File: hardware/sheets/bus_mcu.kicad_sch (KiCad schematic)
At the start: 22 parts, among them U1 RP2350B, U10 74HC163, U11 74HC163, U12 74HC165, U2 74LVC245A, U3 74LVC245A, U4 74LVC245A, U5 74LVC245A, U6 74LVC245A, U7 74HC163, U8 74HC163, U9 74HC163

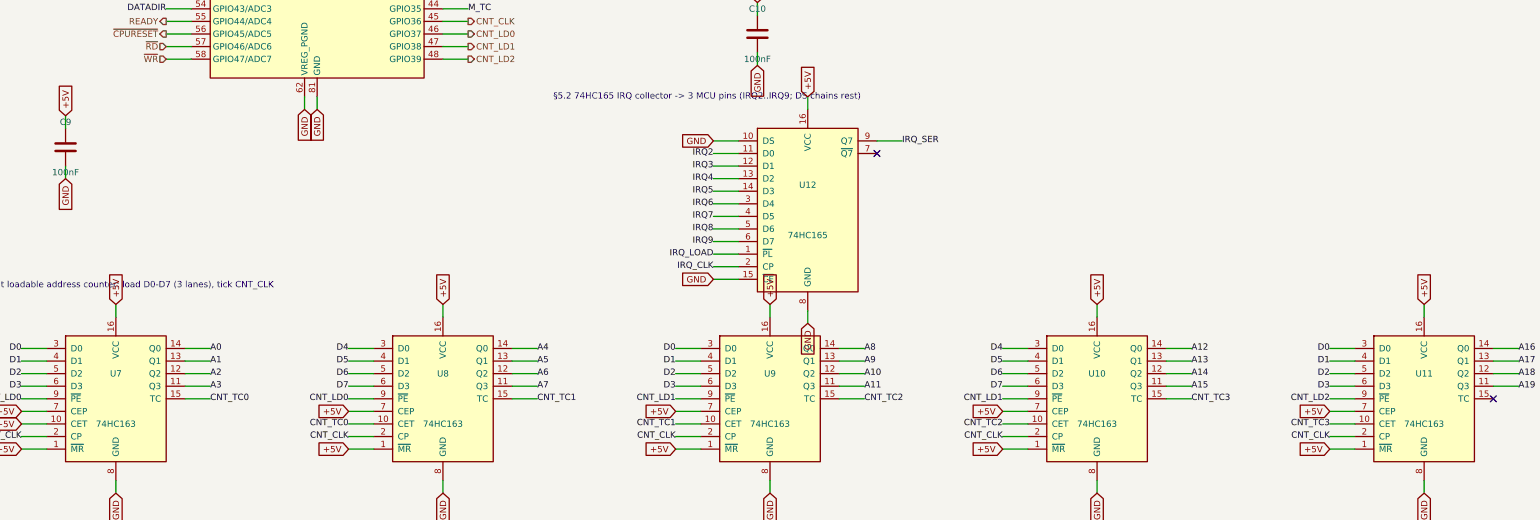
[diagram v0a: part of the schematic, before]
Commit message: Standardize 5V glue on 74HCT; fix bus-latch family; div-3 -> 74HCT163
All 5V 74-series logic moved from mixed HC/HCT to 74HCT (TTL thresholds reliably
read 3.3V level-shifter outputs). Fixes the address latches / data transceiver
that were wrongly 74HC instead of the design's 74HCT. The div-by-3 moves from
74HC4017 (no HCT variant) to a 74HCT163 preset-to-3 with a spare 74HCT04 gate
for the TC->~PE reload. Per-card level shifters use a dedicated 74LVC245A symbol.
Pinouts unchanged; netlist intact; zero structural ERC errors.

Co-Authored-By: Claude Opus 4.8 (1M context) <noreply@anthropic.com>
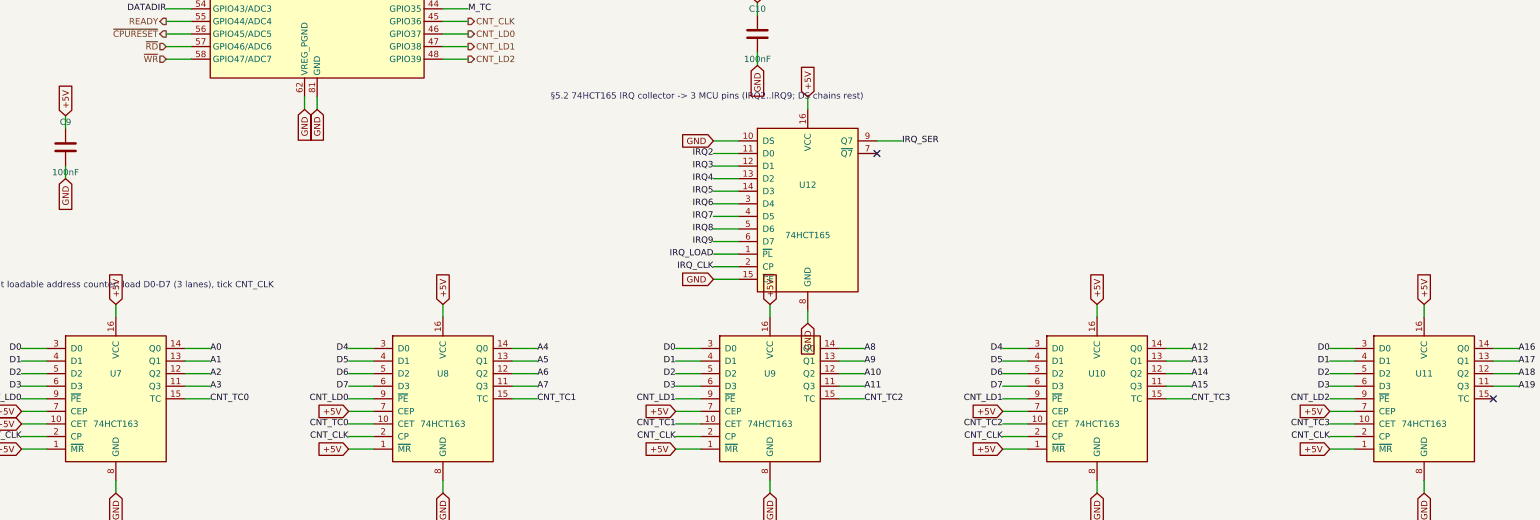
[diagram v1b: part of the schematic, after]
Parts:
- removed U10, U11, U7, U8, U9: 74HC163, symbol mini-xt:74HC163
- removed U12: 74HC165, symbol mini-xt:74HC165
- removed U2, U3, U4, U5, U6: 74LVC245A, symbol mini-xt:74HC245
- added U10, U11, U7, U8, U9: 74HCT163, symbol mini-xt:74HCT163
- added U12: 74HCT165, symbol mini-xt:74HCT165
- added U2, U3, U4, U5, U6: 74LVC245A, symbol mini-xt:74LVC245A
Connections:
- net +3V3: now also U2.20 (VCC), U3.20 (VCC), U4.20 (VCC), U5.20 (VCC), U6.20 (VCC)
- net +5V: now also U10.1 (~{MR}), U10.16 (VCC), U10.7 (CEP), U11.1 (~{MR}), U11.16 (VCC), U11.7 (CEP), U12.16 (VCC), U7.1 (~{MR}), U7.10 (CET), U7.16 (VCC), U7.7 (CEP), U8.1 (~{MR}), U8.16 (VCC), U8.7 (CEP), U9.1 (~{MR}), U9.16 (VCC), U9.7 (CEP)
- net A0: now also U3.18 (B0), U7.14 (Q0)
- net A1: now also U3.17 (B1), U7.13 (Q1)
- net A10: now also U4.16 (B2), U9.12 (Q2)
- net A11: now also U4.15 (B3), U9.11 (Q3)
- net A12: now also U10.14 (Q0), U4.14 (B4)
- net A13: now also U10.13 (Q1), U4.13 (B5)
- net A14: now also U10.12 (Q2), U4.12 (B6)
- net A15: now also U10.11 (Q3), U4.11 (B7)
- net A16: now also U11.14 (Q0), U5.18 (B0)
- net A17: now also U11.13 (Q1), U5.17 (B1)
- net A18: now also U11.12 (Q2), U5.16 (B2)
- net A19: now also U11.11 (Q3), U5.15 (B3)
- net A2: now also U3.16 (B2), U7.12 (Q2)
- net A3: now also U3.15 (B3), U7.11 (Q3)
- net A4: now also U3.14 (B4), U8.14 (Q0)
- net A5: now also U3.13 (B5), U8.13 (Q1)
- net A6: now also U3.12 (B6), U8.12 (Q2)
- net A7: now also U3.11 (B7), U8.11 (Q3)
- net A8: now also U4.18 (B0), U9.14 (Q0)
- net A9: now also U4.17 (B1), U9.13 (Q1)
- net AEN: now also U6.14 (B4)
- net BALE: now also U6.11 (B7)
- net BUSDIR: now also U3.1 (A->B), U4.1 (A->B), U5.1 (A->B), U6.1 (A->B)
- net CNT_CLK: now also U10.2 (CP), U11.2 (CP), U7.2 (CP), U8.2 (CP), U9.2 (CP)
- net CNT_LD0: now also U7.9 (~{PE}), U8.9 (~{PE})
- net CNT_LD1: now also U10.9 (~{PE}), U9.9 (~{PE})
- net CNT_LD2: now also U11.9 (~{PE})
- net CNT_TC0: now also U7.15 (TC), U8.10 (CET)
- net CNT_TC1: now also U8.15 (TC), U9.10 (CET)
- net CNT_TC2: now also U10.10 (CET), U9.15 (TC)
- net CNT_TC3: now also U10.15 (TC), U11.10 (CET)
- net D0: now also U11.3 (D0), U2.18 (B0), U7.3 (D0), U9.3 (D0)
- net D1: now also U11.4 (D1), U2.17 (B1), U7.4 (D1), U9.4 (D1)
- net D2: now also U11.5 (D2), U2.16 (B2), U7.5 (D2), U9.5 (D2)
- net D3: now also U11.6 (D3), U2.15 (B3), U7.6 (D3), U9.6 (D3)
- net D4: now also U10.3 (D0), U2.14 (B4), U8.3 (D0)
- net D5: now also U10.4 (D1), U2.13 (B5), U8.4 (D1)
- net D6: now also U10.5 (D2), U2.12 (B6), U8.5 (D2)
- net D7: now also U10.6 (D3), U2.11 (B7), U8.6 (D3)
- net DATADIR: now also U2.1 (A->B)
- net GND: now also U10.8 (GND), U11.8 (GND), U12.10 (DS), U12.15 (~{CE}), U12.8 (GND), U2.10 (GND), U2.19 (CE), U3.10 (GND), U3.19 (CE), U4.10 (GND), U4.19 (CE), U5.10 (GND), U5.19 (CE), U6.10 (GND), U6.19 (CE), U7.8 (GND), U8.8 (GND), U9.8 (GND)
- net IRQ2: now also U12.11 (D0)
- net IRQ3: now also U12.12 (D1)
- net IRQ4: now also U12.13 (D2)
- net IRQ5: now also U12.14 (D3)
- net IRQ6: now also U12.3 (D4)
- net IRQ7: now also U12.4 (D5)
- net IRQ8: now also U12.5 (D6)
- net IRQ9: now also U12.6 (D7)
- net IRQ_CLK: now also U12.2 (CP)
- net IRQ_LOAD: now also U12.1 (~{PL})
- net IRQ_SER: now also U12.9 (Q7)
- net MA0: now also U3.2 (A0)
- net MA1: now also U3.3 (A1)
- net MA10: now also U4.4 (A2)
- net MA11: now also U4.5 (A3)
- net MA12: now also U4.6 (A4)
- net MA13: now also U4.7 (A5)
- net MA14: now also U4.8 (A6)
- net MA15: now also U4.9 (A7)
- net MA16: now also U5.2 (A0)
- net MA17: now also U5.3 (A1)
- net MA18: now also U5.4 (A2)
- net MA19: now also U5.5 (A3)
- net MA2: now also U3.4 (A2)
- net MA3: now also U3.5 (A3)
- net MA4: now also U3.6 (A4)
- net MA5: now also U3.7 (A5)
- net MA6: now also U3.8 (A6)
- net MA7: now also U3.9 (A7)
- net MA8: now also U4.2 (A0)
- net MA9: now also U4.3 (A1)
- net MD0: now also U2.2 (A0)
- net MD1: now also U2.3 (A1)
- net MD2: now also U2.4 (A2)
- net MD3: now also U2.5 (A3)
- net MD4: now also U2.6 (A4)
- net MD5: now also U2.7 (A5)
- net MD6: now also U2.8 (A6)
- net MD7: now also U2.9 (A7)
- net M_AEN: now also U6.6 (A4)
- net M_BALE: now also U6.9 (A7)
- net M_IOR: now also U6.2 (A0)
- net M_IOW: now also U6.3 (A1)
- net M_MEMR: now also U6.4 (A2)
- net M_MEMW: now also U6.5 (A3)
- net M_RESETDRV: now also U6.7 (A5)
- net M_TC: now also U6.8 (A6)
- net RESET_DRV: now also U6.13 (B5)
- net TC: now also U6.12 (B6)
- net ~{IOR}: now also U6.18 (B0)
- net ~{IOW}: now also U6.17 (B1)
- net ~{MEMR}: now also U6.16 (B2)
- net ~{MEMW}: now also U6.15 (B3)
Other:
- note added: "§5.2 74HCT165 IRQ collector -> 3 MCU pins (IRQ2..IRQ9; DS chains rest)"
- note removed: "§5.2 74HC165 IRQ collector -> 3 MCU pins (IRQ2..IRQ9; DS chains rest)"
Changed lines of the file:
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@@
 		(at 214.63 222.25)
 	)
-	(text "§5.2 74HC165 IRQ collector -> 3 MCU pins (IRQ2..IRQ9; DS chains rest)"
+	(text "§5.2 74HCT165 IRQ collector -> 3 MCU pins (IRQ2..IRQ9; DS chains rest)"
 		(at 180.34 210.82 0)
 		(effects
@@
 		(instances
 			(project "mini-xt"
-				(path "/d5fb706d-3720-437f-850e-91a8fdce298f/59d1bc93-8348-4a37-b005-a2b2152d1bab"
+				(path "/12a90590-121b-4b08-bc73-62c223de1072/e50d0a17-50fb-4006-9356-a8363e32698a"
 					(reference "U201")
 					(unit 1)
@@
 	)
 	(symbol
-		(lib_id "mini-xt:74HC245")
+		(lib_id "mini-xt:74LVC245A")
 		(at 200.66 76.2 0)
 		(unit 1)
@@
 		(instances
 			(project "mini-xt"
-				(path "/d5fb706d-3720-437f-850e-91a8fdce298f/59d1bc93-8348-4a37-b005-a2b2152d1bab"
+				(path "/12a90590-121b-4b08-bc73-62c223de1072/e50d0a17-50fb-4006-9356-a8363e32698a"
 					(reference "U202")
 					(unit 1)
@@
 	)
 	(symbol
-		(lib_id "mini-xt:74HC245")
+		(lib_id "mini-xt:74LVC245A")
 		(at 200.66 152.4 0)
 		(unit 1)
@@
 		(instances
 			(project "mini-xt"
-				(path "/d5fb706d-3720-437f-850e-91a8fdce298f/59d1bc93-8348-4a37-b005-a2b2152d1bab"
+				(path "/12a90590-121b-4b08-bc73-62c223de1072/e50d0a17-50fb-4006-9356-a8363e32698a"
 					(reference "U206")
 					(unit 1)
@@
 	)
 	(symbol
-		(lib_id "mini-xt:74HC245")
+		(lib_id "mini-xt:74LVC245A")
 		(at 281.94 76.2 0)
 		(unit 1)
@@
 		(instances
 			(project "mini-xt"
-				(path "/d5fb706d-3720-437f-850e-91a8fdce298f/59d1bc93-8348-4a37-b005-a2b2152d1bab"
+				(path "/12a90590-121b-4b08-bc73-62c223de1072/e50d0a17-50fb-4006-9356-a8363e32698a"
 					(reference "U203")
 					(unit 1)
@@
 	)
 	(symbol
-		(lib_id "mini-xt:74HC245")
+		(lib_id "mini-xt:74LVC245A")
 		(at 358.14 76.2 0)
 		(unit 1)
@@
 		(instances
 			(project "mini-xt"
-				(path "/d5fb706d-3720-437f-850e-91a8fdce298f/59d1bc93-8348-4a37-b005-a2b2152d1bab"
+				(path "/12a90590-121b-4b08-bc73-62c223de1072/e50d0a17-50fb-4006-9356-a8363e32698a"
 					(reference "U204")
 					(unit 1)
@@
 	)
 	(symbol
-		(lib_id "mini-xt:74HC245")
+		(lib_id "mini-xt:74LVC245A")
 		(at 281.94 152.4 0)
 		(unit 1)
@@
 		(instances
 			(project "mini-xt"
-				(path "/d5fb706d-3720-437f-850e-91a8fdce298f/59d1bc93-8348-4a37-b005-a2b2152d1bab"
+				(path "/12a90590-121b-4b08-bc73-62c223de1072/e50d0a17-50fb-4006-9356-a8363e32698a"
 					(reference "U205")
 					(unit 1)
@@
 	)
 	(symbol
-		(lib_id "mini-xt:74HC163")
+		(lib_id "mini-xt:74HCT163")
 		(at 60.96 271.78 0)
 		(unit 1)
@@
 			)
 		)
-		(property "Value" "74HC163"
+		(property "Value" "74HCT163"
 			(at 60.96 276.86 0)
 			(effects
@@
 		(instances
 			(project "mini-xt"
-				(path "/d5fb706d-3720-437f-850e-91a8fdce298f/59d1bc93-8348-4a37-b005-a2b2152d1bab"
+				(path "/12a90590-121b-4b08-bc73-62c223de1072/e50d0a17-50fb-4006-9356-a8363e32698a"
 					(reference "U207")
 					(unit 1)
@@
 	)
 	(symbol
-		(lib_id "mini-xt:74HC163")
+		(lib_id "mini-xt:74HCT163")
 		(at 127 271.78 0)
 		(unit 1)
@@
 			)
 		)
-		(property "Value" "74HC163"
+		(property "Value" "74HCT163"
 			(at 127 276.86 0)
 			(effects
@@
 		(instances
 			(project "mini-xt"
-				(path "/d5fb706d-3720-437f-850e-91a8fdce298f/59d1bc93-8348-4a37-b005-a2b2152d1bab"
+				(path "/12a90590-121b-4b08-bc73-62c223de1072/e50d0a17-50fb-4006-9356-a8363e32698a"
 					(reference "U208")
 					(unit 1)
@@
 	)
 	(symbol
-		(lib_id "mini-xt:74HC163")
+		(lib_id "mini-xt:74HCT163")
 		(at 193.04 271.78 0)
 		(unit 1)
@@
 			)
 		)
-		(property "Value" "74HC163"
+		(property "Value" "74HCT163"
 			(at 193.04 276.86 0)
 			(effects
@@
 		(instances
 			(project "mini-xt"
-				(path "/d5fb706d-3720-437f-850e-91a8fdce298f/59d1bc93-8348-4a37-b005-a2b2152d1bab"
+				(path "/12a90590-121b-4b08-bc73-62c223de1072/e50d0a17-50fb-4006-9356-a8363e32698a"
 					(reference "U209")
 					(unit 1)
@@
 	)
 	(symbol
-		(lib_id "mini-xt:74HC163")
+		(lib_id "mini-xt:74HCT163")
 		(at 259.08 271.78 0)
 		(unit 1)
@@
 			)
 		)
-		(property "Value" "74HC163"
+		(property "Value" "74HCT163"
 			(at 259.08 276.86 0)
 			(effects
@@
 		(instances
 			(project "mini-xt"
-				(path "/d5fb706d-3720-437f-850e-91a8fdce298f/59d1bc93-8348-4a37-b005-a2b2152d1bab"
+				(path "/12a90590-121b-4b08-bc73-62c223de1072/e50d0a17-50fb-4006-9356-a8363e32698a"
 					(reference "U210")
 					(unit 1)
@@
 	)
 	(symbol
-		(lib_id "mini-xt:74HC163")
+		(lib_id "mini-xt:74HCT163")
 		(at 325.12 271.78 0)
 		(unit 1)
@@
 			)
 		)
-		(property "Value" "74HC163"
+		(property "Value" "74HCT163"
 			(at 325.12 276.86 0)
 			(effects
@@
 		(instances
 			(project "mini-xt"
-				(path "/d5fb706d-3720-437f-850e-91a8fdce298f/59d1bc93-8348-4a37-b005-a2b2152d1bab"
+				(path "/12a90590-121b-4b08-bc73-62c223de1072/e50d0a17-50fb-4006-9356-a8363e32698a"
 					(reference "U211")
 					(unit 1)
@@
 	)
 	(symbol
-		(lib_id "mini-xt:74HC165")
+		(lib_id "mini-xt:74HCT165")
 		(at 200.66 233.68 0)
 		(unit 1)
@@
 			)
 		)
-		(property "Value" "74HC165"
+		(property "Value" "74HCT165"
 			(at 200.66 238.76 0)
 			(effects
@@
 		(instances
 			(project "mini-xt"
-				(path "/d5fb706d-3720-437f-850e-91a8fdce298f/59d1bc93-8348-4a37-b005-a2b2152d1bab"
+				(path "/12a90590-121b-4b08-bc73-62c223de1072/e50d0a17-50fb-4006-9356-a8363e32698a"
 					(reference "U212")
 					(unit 1)
@@
 		(instances
 			(project "mini-xt"
-				(path "/d5fb706d-3720-437f-850e-91a8fdce298f/59d1bc93-8348-4a37-b005-a2b2152d1bab"
+				(path "/12a90590-121b-4b08-bc73-62c223de1072/e50d0a17-50fb-4006-9356-a8363e32698a"
 					(reference "C201")
 					(unit 1)
@@
 		(instances
 			(project "mini-xt"
-				(path "/d5fb706d-3720-437f-850e-91a8fdce298f/59d1bc93-8348-4a37-b005-a2b2152d1bab"
+				(path "/12a90590-121b-4b08-bc73-62c223de1072/e50d0a17-50fb-4006-9356-a8363e32698a"
 					(reference "C202")
 					(unit 1)
@@
 		(instances
 			(project "mini-xt"
-				(path "/d5fb706d-3720-437f-850e-91a8fdce298f/59d1bc93-8348-4a37-b005-a2b2152d1bab"
+				(path "/12a90590-121b-4b08-bc73-62c223de1072/e50d0a17-50fb-4006-9356-a8363e32698a"
 					(reference "C203")
 					(unit 1)
@@
 		(instances
 			(project "mini-xt"
-				(path "/d5fb706d-3720-437f-850e-91a8fdce298f/59d1bc93-8348-4a37-b005-a2b2152d1bab"
+				(path "/12a90590-121b-4b08-bc73-62c223de1072/e50d0a17-50fb-4006-9356-a8363e32698a"
 					(reference "C204")
 					(unit 1)
@@
 		(instances
 			(project "mini-xt"
-				(path "/d5fb706d-3720-437f-850e-91a8fdce298f/59d1bc93-8348-4a37-b005-a2b2152d1bab"
+				(path "/12a90590-121b-4b08-bc73-62c223de1072/e50d0a17-50fb-4006-9356-a8363e32698a"
 					(reference "C205")
 					(unit 1)
@@
 		(instances
 			(project "mini-xt"
-				(path "/d5fb706d-3720-437f-850e-91a8fdce298f/59d1bc93-8348-4a37-b005-a2b2152d1bab"
+				(path "/12a90590-121b-4b08-bc73-62c223de1072/e50d0a17-50fb-4006-9356-a8363e32698a"
 					(reference "C206")
 					(unit 1)
@@
 		(instances
 			(project "mini-xt"
-				(path "/d5fb706d-3720-437f-850e-91a8fdce298f/59d1bc93-8348-4a37-b005-a2b2152d1bab"
+				(path "/12a90590-121b-4b08-bc73-62c223de1072/e50d0a17-50fb-4006-9356-a8363e32698a"
 					(reference "C207")
 					(unit 1)
@@
 		(instances
 			(project "mini-xt"
-				(path "/d5fb706d-3720-437f-850e-91a8fdce298f/59d1bc93-8348-4a37-b005-a2b2152d1bab"
+				(path "/12a90590-121b-4b08-bc73-62c223de1072/e50d0a17-50fb-4006-9356-a8363e32698a"
 					(reference "C208")
 					(unit 1)
@@
 		(instances
 			(project "mini-xt"
-				(path "/d5fb706d-3720-437f-850e-91a8fdce298f/59d1bc93-8348-4a37-b005-a2b2152d1bab"
+				(path "/12a90590-121b-4b08-bc73-62c223de1072/e50d0a17-50fb-4006-9356-a8363e32698a"
 					(reference "C209")
 					(unit 1)
@@
 		(instances
 			(project "mini-xt"
-				(path "/d5fb706d-3720-437f-850e-91a8fdce298f/59d1bc93-8348-4a37-b005-a2b2152d1bab"
+				(path "/12a90590-121b-4b08-bc73-62c223de1072/e50d0a17-50fb-4006-9356-a8363e32698a"
 					(reference "C210")
 					(unit 1)
